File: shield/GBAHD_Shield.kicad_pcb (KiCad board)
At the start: 2 copper layers, 49 x 39 mm, 18 parts, among them J1 Conn_01x40, J2 Conn_02x08_Top_Bottom, J3 Conn_01x16, J4 Conn_02x10_Top_Bottom, J5 Conn_01x05, J6 Conn_02x03_Odd_Even, J7 Conn_01x01, SW1 SW_Push, U1 SNES_7PIN, U2 ATmega328P-AU, U3 WAS3157B, X1 Crystal_GND2

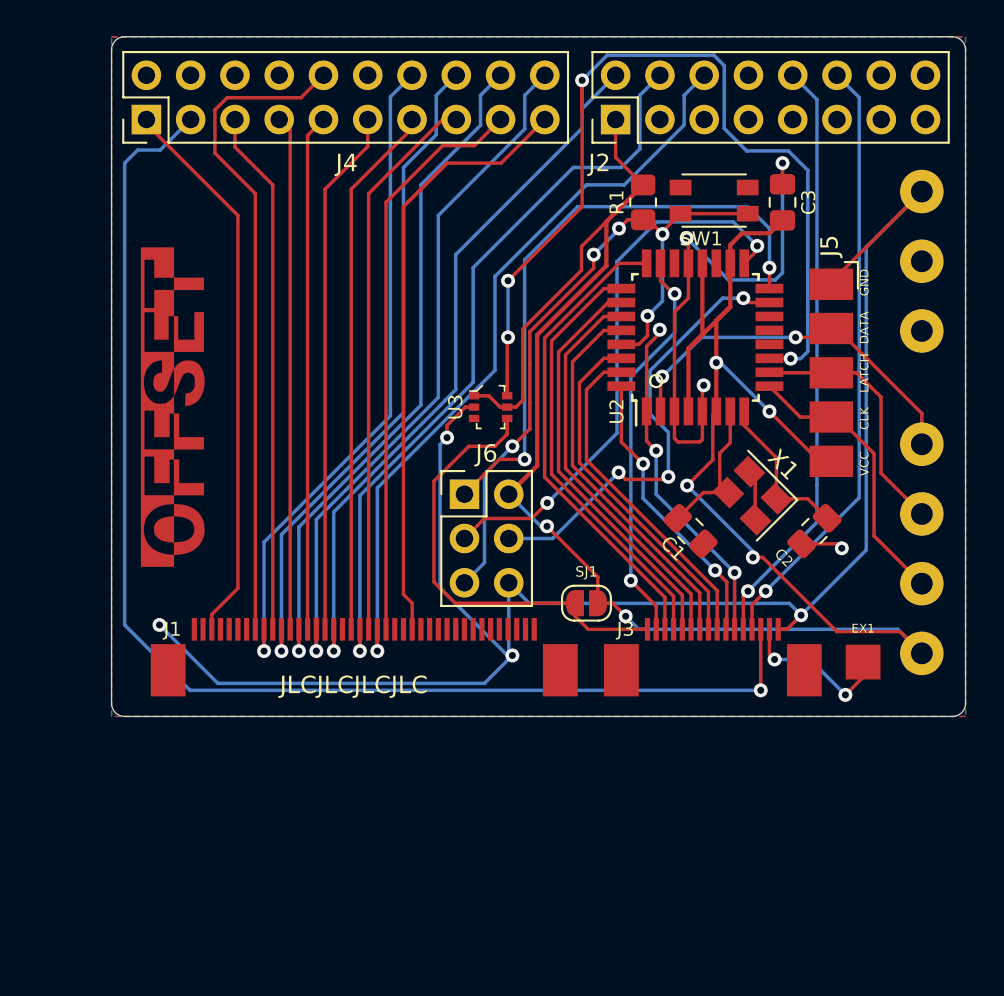
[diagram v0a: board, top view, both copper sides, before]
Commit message: Updated shield PCB and readme
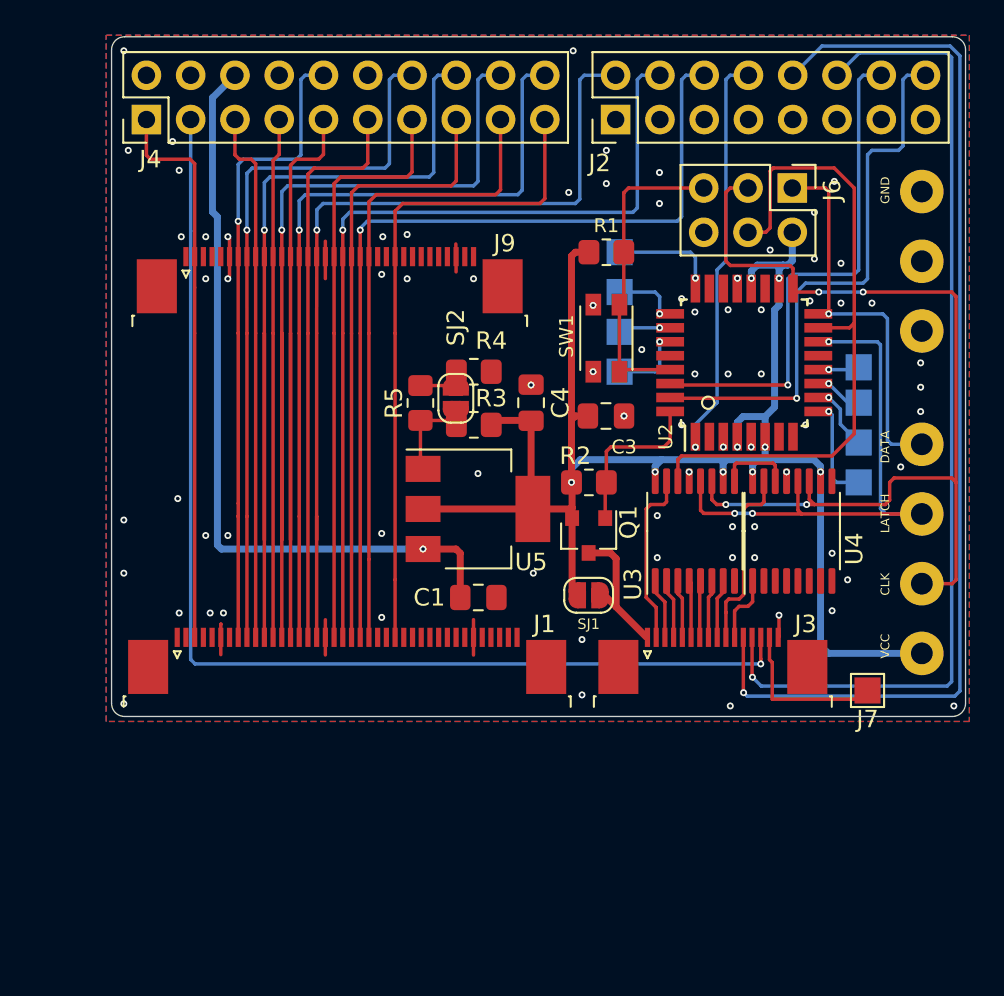
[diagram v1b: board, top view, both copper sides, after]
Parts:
- removed C2: 22pF, Capacitor_SMD:C_0805_2012Metric_Pad1.18x1.45mm_HandSolder
- removed G***: LOGO, OFFSET:OFFSET_LOGO_4.0mm
- removed X1: Crystal_GND2, Crystal:Crystal_SMD_3225-4Pin_3.2x2.5mm
- added C4: 22u, Capacitor_SMD:C_0805_2012Metric_Pad1.18x1.45mm_HandSolder, F.Cu at (68.1, 47.5)
- added J10: Conn_01x01, TestPoint:TestPoint_Pad_1.5x1.5mm, B.Cu at (73.2, 41.1)
- added J11: Conn_01x01, TestPoint:TestPoint_Pad_1.5x1.5mm, B.Cu at (73.2, 45.7)
- added J12: Conn_01x01, TestPoint:TestPoint_Pad_1.5x1.5mm, B.Cu at (86.9, 52.1)
- added J13: Conn_01x01, TestPoint:TestPoint_Pad_1.5x1.5mm, B.Cu at (86.9, 47.5)
- added J15: Conn_01x01, TestPoint:TestPoint_Pad_1.5x1.5mm, B.Cu at (73.2, 38.9)
- added J16: Conn_01x01, TestPoint:TestPoint_Pad_1.5x1.5mm, B.Cu at (73.2, 43.4)
- added J18: Conn_01x01, TestPoint:TestPoint_Pad_1.5x1.5mm, B.Cu at (86.9, 49.8)
- added J9: FLEX_GBA-SP, Connector_FFC-FPC:TE_3-1734839-4_1x34-1MP_P0.5mm_Horizontal, F.Cu at (56.5, 40.5)
- added Q1: Q_PMOS_GSD, Package_TO_SOT_SMD:SOT-23, F.Cu at (71.4, 55.1)
- added R2: 10K, Resistor_SMD:R_0805_2012Metric_Pad1.20x1.40mm_HandSolder, F.Cu at (71.4, 52.1)
- added R3: 10K, Resistor_SMD:R_0805_2012Metric_Pad1.20x1.40mm_HandSolder, F.Cu at (64.8, 48.8)
- added R4: 16.2K, Resistor_SMD:R_0805_2012Metric_Pad1.20x1.40mm_HandSolder, F.Cu at (64.8, 45.7)
- added R5: 7.5K, Resistor_SMD:R_0805_2012Metric_Pad1.20x1.40mm_HandSolder, F.Cu at (61.7, 47.5)
- added SJ2: SOLDER_JUMPER, Jumper:SolderJumper-2_P1.3mm_Open_RoundedPad1.0x1.5mm, F.Cu at (63.8, 47.2)
- added U4: 74HC595, Package_SO:TSSOP-16_4.4x5mm_P0.65mm, F.Cu at (83.1, 54.9)
- added U5: AMS1117, Package_TO_SOT_SMD:SOT-223-3_TabPin2, F.Cu at (65.0, 53.6)
- C1: value 22pF -> 100nF
- J1: value Conn_01x40 -> FFC_OGBA; footprint OFFSET:JUSHUO_AFC07-S40FCC-00 -> Connector_FFC-FPC:TE_4-1734839-0_1x40-1MP_P0.5mm_Horizontal
- J3: footprint OFFSET:JUSHUO_AFC07-S16FCC-00 -> Connector_FFC-FPC:TE_1-1734839-6_1x16-1MP_P0.5mm_Horizontal
- J5: value Conn_01x05 -> Conn_01x01; footprint OFFSET:Pads_01x05 -> TestPoint:TestPoint_Pad_1.5x1.5mm; moved to B.Cu
- J7: footprint OFFSET:SOLDER_PAD -> TestPoint:TestPoint_Pad_1.5x1.5mm
- U3: value WAS3157B -> 74HC595; footprint OFFSET:SOT-363 -> Package_SO:TSSOP-16_4.4x5mm_P0.65mm
- moved J6 25.7 mm to (83.1, 35.2), turned to 270 degrees
- moved C3 15.9 mm to (72.4, 48.3), turned to 180 degrees
- moved U3 13.7 mm to (77.5, 54.9), turned to 90 degrees
- moved C1 12.8 mm to (65.0, 58.7), turned to 180 degrees
- moved SW1 10.0 mm to (72.4, 43.8), turned to 270 degrees
- moved R1 3.56 mm to (72.4, 38.9), turned to 0 degrees
- moved U2 3.15 mm to (80.3, 45.2)
- moved J5 1.89 mm to (86.9, 45.5), turned to 0 degrees
- moved J7 1.80 mm to (87.4, 64.0), turned to 180 degrees
- moved J1 0.76 mm to (57.5, 62.3)
- moved SJ1 0.47 mm to (71.4, 58.5)
- moved J3 0.06 mm to (78.5, 62.3)
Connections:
- C1 pad 2: Net-(C1-Pad2) -> +5V
- C3 pad 2: SP_3V3 -> VCC
- J1 pad 1: Net-(J1-Pad1) -> (no net)
- J1 pad 18: Net-(J1-Pad18) -> GND
- J1 pad 2: Net-(J1-Pad2) -> (no net)
- J1 pad 24: Net-(J1-Pad24) -> (no net)
- J1 pad 25: Net-(J1-Pad25) -> (no net)
- J1 pad 27: Net-(J1-Pad27) -> (no net)
- J1 pad 28: Net-(J1-Pad28) -> (no net)
- J1 pad 29: Net-(J1-Pad29) -> (no net)
- J1 pad 30: Net-(J1-Pad30) -> (no net)
- J1 pad 31: Net-(J1-Pad31) -> (no net)
- J1 pad 32: Net-(J1-Pad32) -> (no net)
- J1 pad 33: Net-(J1-Pad33) -> (no net)
- J1 pad 34: Net-(J1-Pad34) -> (no net)
- J1 pad 35: Net-(J1-Pad35) -> GND
- J1 pad 36: Net-(J1-Pad36) -> (no net)
- J1 pad 37: Net-(J1-Pad37) -> (no net)
- J1 pad 38: Net-(J1-Pad38) -> (no net)
- J1 pad 39: Net-(J1-Pad39) -> (no net)
- J1 pad 4: Net-(J1-Pad4) -> (no net)
- J1 pad 40: Net-(J1-Pad40) -> (no net)
- J1 pad 5: Net-(J1-Pad5) -> (no net)
- J1 pad 6: Net-(J1-Pad6) -> GND
- J1 pad 7: Net-(J1-Pad7) -> (no net)
- J2 pad 1: SP_3V3 -> (no net)
- J2 pad 11: Net-(J2-Pad11) -> (no net)
- J2 pad 13: Net-(J2-Pad13) -> (no net)
- J2 pad 15: Net-(J2-Pad15) -> (no net)
- J2 pad 16: SP_ARD0 -> RX
- J2 pad 5: Net-(J2-Pad5) -> (no net)
- J2 pad 7: Net-(J2-Pad7) -> (no net)
- J2 pad 8: SP_ARD4 -> PIXEL_GRID
- J2 pad 9: Net-(J2-Pad9) -> (no net)
- J4 pad 12: SP_ARD12 -> (no net)
- J4 pad 2: SP_ARD17 -> (no net)
- J4 pad 4: SP_ARD16 -> (no net)
- J4 pad 6: SP_ARD15 -> +5V
- J4 pad 8: SP_ARD14 -> (no net)
- J5 pad 1: GND -> Net-(J5-Pad1)
- J6 pad 2: SP_3V3 -> VCC
- R1 pad 1: SP_3V3 -> VCC
- SJ1 pad 1: GBA_VCC -> VCC
- SJ1 pad 2: SP_3V3 -> GBA_VCC
- U1 pad 1: SP_3V3 -> VCC
- U1 pad 2: SNS_CLK -> ICSP_SCK
- U1 pad 4: SNS_DATA -> ICSP_MISO
- U2 pad 1: GBA_SELECT -> PIXEL_GRID
- U2 pad 10: SNS_LATCH -> Net-(J18-Pad1)
- U2 pad 11: GBA_POWER_SEL -> Net-(J13-Pad1)
- U2 pad 12: Net-(U2-Pad12) -> Net-(J5-Pad1)
- U2 pad 13: Net-(U2-Pad13) -> (no net)
- U2 pad 14: Net-(U2-Pad14) -> SNS_LATCH
- U2 pad 18: SP_3V3 -> VCC
- U2 pad 19: Net-(U2-Pad19) -> (no net)
- U2 pad 2: SNS_DATA -> (no net)
- U2 pad 20: SP_3V3 -> VCC
- U2 pad 22: Net-(U2-Pad22) -> (no net)
- U2 pad 23: GBA_UP -> (no net)
- U2 pad 24: GBA_DOWN -> Net-(J15-Pad1)
- U2 pad 25: GBA_LEFT -> Net-(J10-Pad1)
- U2 pad 26: GBA_RGHT -> Net-(J16-Pad1)
- U2 pad 27: GBA_A -> Net-(J11-Pad1)
- U2 pad 28: GBA_B -> (no net)
- U2 pad 30: GBA_L -> SP_ARD1
- U2 pad 31: GBA_R -> RX
- U2 pad 32: GBA_START -> GBA_POWER_SEL
- U2 pad 4: SP_3V3 -> VCC
- U2 pad 6: SP_3V3 -> VCC
- U2 pad 7: Net-(C1-Pad2) -> (no net)
- U2 pad 8: Net-(C2-Pad2) -> (no net)
- U2 pad 9: SNS_CLK -> Net-(J12-Pad1)
- U3 pad 1: SP_3V3 -> GBA_DOWN
- U3 pad 2: GND -> GBA_LEFT
- U3 pad 3: Net-(U3-Pad3) -> GBA_RGHT
- U3 pad 4: GBA_VCC -> GBA_A
- U3 pad 5: SP_3V3 -> GBA_B
- U3 pad 6: GBA_POWER_SEL -> GBA_L
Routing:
- net SP_3V3: track 126.4 -> 0.00 mm, vias 6 -> 0
- net GND: track 134.3 -> 13.1 mm, vias 8 -> 78
- net VCC: track 0.00 -> 91.3 mm, vias 0 -> 9
- net +5V: track 0.00 -> 44.3 mm, vias 0 -> 1
- net GBA_POWER_SEL: track 52.9 -> 9.45 mm, vias 4 -> 0
- net RX: track 0.00 -> 32.3 mm, vias 0 -> 1
- net SP_ARD1: track 0.00 -> 29.5 mm, vias 0 -> 1
- net GBA_AUD2: track 34.1 -> 62.8 mm
- net ICSP_SCK: track 32.0 -> 56.3 mm, vias 2 -> 4
- net GBA_DOWN: track 27.2 -> 3.46 mm
- net PIXEL_GRID: track 0.00 -> 23.2 mm, vias 0 -> 1
- net AT_RST: track 40.4 -> 18.0 mm, vias 5 -> 0
- net GBA_AUD1: track 34.9 -> 57.1 mm
- net SNS_DATA: track 21.9 -> 0.00 mm, vias 2 -> 0
- net GBA_LEFT: track 24.7 -> 3.40 mm
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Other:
- net class Default: via_dia 0.8 -> 0.4; via_drill 0.4 -> 0.2
- net class VCC: trace_width 0.25 -> 0.4; via_dia 0.8 -> 0.4; via_drill 0.4 -> 0.2
- rule via_min_drill: 0.3 -> 0.2
- board text added: "Designed in Germany"
- board text added: "ManCloud 2021"
- board text added: "v20210318"
- board text removed: "Designed in México"
- board text removed: "EX1"
- board text removed: "JLCJLCJLCJLC"
- board text removed: "Raizu 2020"

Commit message: Updated to "Full-Shield"
* changed supplies to 3V3 and 4V0
* added pads for BAT connection
* added 32-Pin FFC Connector
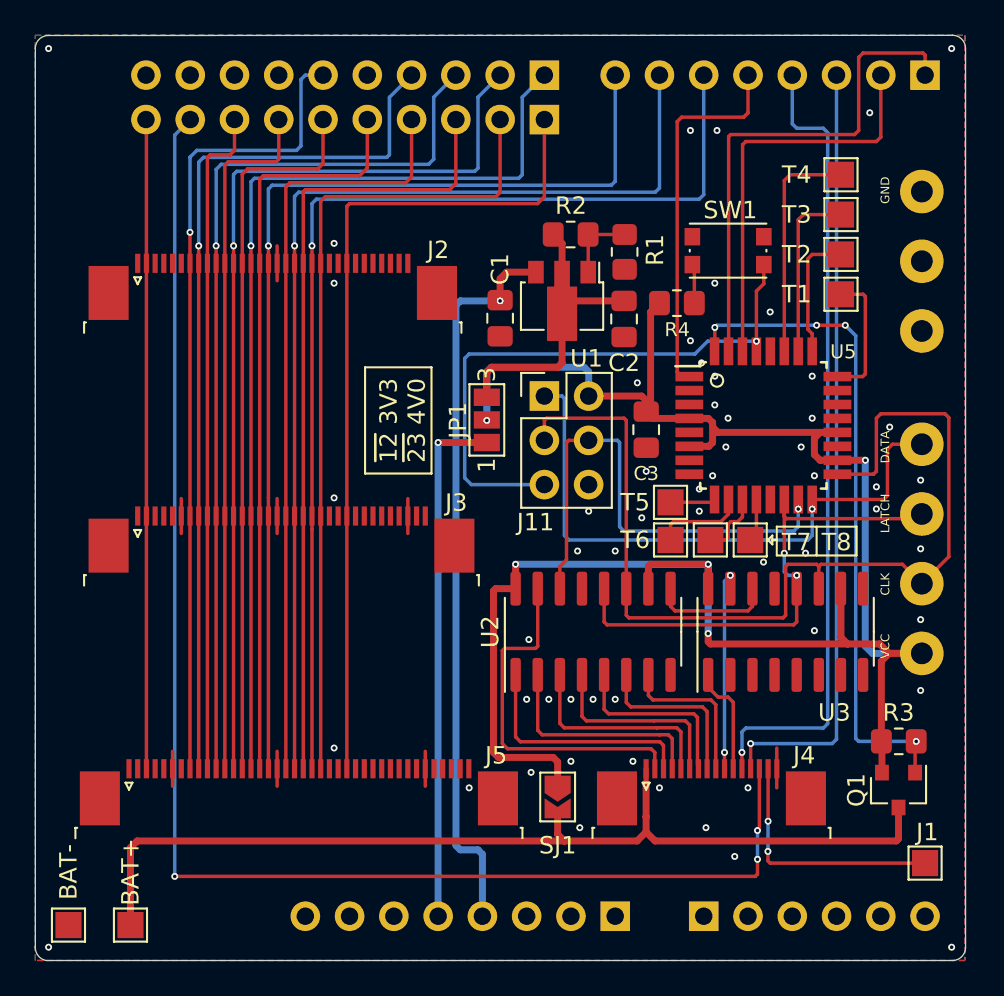
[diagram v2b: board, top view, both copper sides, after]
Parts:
- removed C4: 22u, Capacitor_SMD:C_0805_2012Metric_Pad1.18x1.45mm_HandSolder
- removed J12, J13, J16, J18: Conn_01x01, TestPoint:TestPoint_Pad_1.5x1.5mm
- removed the R3 at (64.8, 48.8)
- removed the R4 at (64.8, 45.7)
- removed R5: 7.5K, Resistor_SMD:R_0805_2012Metric_Pad1.20x1.40mm_HandSolder
- removed SJ2: SOLDER_JUMPER, Jumper:SolderJumper-2_P1.3mm_Open_RoundedPad1.0x1.5mm
- removed the U4 at (83.1, 54.9)
- added BAT+: Conn_01x01, TestPoint:TestPoint_Pad_1.5x1.5mm, F.Cu at (45.1, 77.5)
- added BAT-: Conn_01x01, TestPoint:TestPoint_Pad_1.5x1.5mm, F.Cu at (41.5, 77.5)
- added C2: 22u, Capacitor_SMD:C_0805_2012Metric_Pad1.18x1.45mm_HandSolder, F.Cu at (73.4, 42.7)
- added J6: Conn_01x06, Connector_PinHeader_2.54mm:PinHeader_1x06_P2.54mm_Vertical, B.Cu at (78.0, 77.0)
- added J7: Conn_01x08, Connector_PinHeader_2.54mm:PinHeader_1x08_P2.54mm_Vertical, B.Cu at (72.9, 77.0)
- added J8: Conn_01x10, Connector_PinHeader_2.54mm:PinHeader_1x10_P2.54mm_Vertical, B.Cu at (68.8, 31.2)
- added JP1: SolderJumper_3_Open, Jumper:SolderJumper-3_P1.3mm_Open_Pad1.0x1.5mm_NumberLabels, F.Cu at (65.5, 48.5)
- added R1: 2.2k, Resistor_SMD:R_0805_2012Metric_Pad1.20x1.40mm_HandSolder, F.Cu at (73.4, 38.8)
- added R2: 1k, Resistor_SMD:R_0805_2012Metric_Pad1.20x1.40mm_HandSolder, F.Cu at (70.3, 37.8)
- added T2: Conn_01x01, TestPoint:TestPoint_Pad_1.5x1.5mm, F.Cu at (85.9, 39.0)
- added T3: Conn_01x01, TestPoint:TestPoint_Pad_1.5x1.5mm, F.Cu at (85.9, 36.7)
- added T5: Conn_01x01, TestPoint:TestPoint_Pad_1.5x1.5mm, F.Cu at (76.1, 53.2)
- added T6: Conn_01x01, TestPoint:TestPoint_Pad_1.5x1.5mm, F.Cu at (76.1, 55.4)
- added T7: Conn_01x01, TestPoint:TestPoint_Pad_1.5x1.5mm, F.Cu at (78.4, 55.4)
- added U1: AZ1117R-ADJ, Package_TO_SOT_SMD:SOT-89-3, F.Cu at (69.8, 41.7)
- J10: value Conn_01x01 -> Conn_01x10; footprint TestPoint:TestPoint_Pad_1.5x1.5mm -> Connector_PinHeader_2.54mm:PinHeader_1x10_P2.54mm_Vertical
- J2: value Conn_02x08_Top_Bottom -> FFC_OGBA_32; footprint Connector_PinHeader_2.54mm:PinHeader_2x08_P2.54mm_Vertical -> Connector_FFC-FPC:TE_3-1734839-2_1x32-1MP_P0.5mm_Horizontal
- J3: value Conn_01x16 -> FFC_GBA-SP; footprint Connector_FFC-FPC:TE_1-1734839-6_1x16-1MP_P0.5mm_Horizontal -> Connector_FFC-FPC:TE_3-1734839-4_1x34-1MP_P0.5mm_Horizontal
- J4: value Conn_02x10_Top_Bottom -> Conn_01x16; footprint Connector_PinHeader_2.54mm:PinHeader_2x10_P2.54mm_Vertical -> Connector_FFC-FPC:TE_1-1734839-6_1x16-1MP_P0.5mm_Horizontal
- J5: renamed from J1; value FFC_OGBA -> FFC_OGBA_40
- J9: value FLEX_GBA-SP -> Conn_01x08; footprint Connector_FFC-FPC:TE_3-1734839-4_1x34-1MP_P0.5mm_Horizontal -> Connector_PinHeader_2.54mm:PinHeader_1x08_P2.54mm_Vertical; moved to B.Cu
- SJ1: footprint Jumper:SolderJumper-2_P1.3mm_Open_RoundedPad1.0x1.5mm -> Jumper:SolderJumper-2_P1.3mm_Open_TrianglePad1.0x1.5mm
- SW1: footprint OFFSET:XKB-TS-1185EC-C-D-B -> Button_Switch_SMD:SW_Push_1P1T_NO_CK_KMR2
- T1: renamed from J15; moved to F.Cu
- T4: renamed from J11; moved to F.Cu
- T8: renamed from J5; moved to F.Cu
- U2: value ATmega328P-AU -> 74HC595; footprint Package_QFP:TQFP-32_7x7mm_P0.8mm -> Package_SO:SOIC-16_3.9x9.9mm_P1.27mm
- U3: footprint Package_SO:TSSOP-16_4.4x5mm_P0.65mm -> Package_SO:SOIC-16_3.9x9.9mm_P1.27mm
- U5: value AMS1117 -> ATmega328P-AU; footprint Package_TO_SOT_SMD:SOT-223-3_TabPin2 -> Package_QFP:TQFP-32_7x7mm_P0.8mm
- moved J4 50.4 mm to (78.4, 69.8), turned to 0 degrees
- moved J9 36.1 mm to (90.7, 28.7), turned to 90 degrees
- moved J3 25.7 mm to (53.8, 55.4)
- moved R3 23.2 mm to (89.2, 66.9)
- moved Q1 23.0 mm to (89.2, 69.7)
- moved J2 21.9 mm to (53.2, 40.9), turned to 0 degrees
- moved J11 18.6 mm to (68.8, 47.1), turned to 0 degrees
- moved U2 17.7 mm to (71.6, 60.6)
- moved U5 17.1 mm to (81.4, 48.8)
- moved T4 17.0 mm to (85.9, 34.4)
- moved C1 16.1 mm to (66.3, 42.7), turned to 90 degrees
- moved J10 13.2 mm to (68.8, 28.7), turned to 90 degrees
- moved T1 12.9 mm to (85.9, 41.3)
- moved SJ1 11.7 mm to (69.6, 70.1), turned to 270 degrees
- moved T8 11.7 mm to (80.6, 55.4)
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- renumbered J7 to J1, J6 to J11, R2 to R3, R1 to R4, U1 to U4
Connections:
- J1 pad 1: Net-(J3-Pad15) -> Net-(J1-Pad1)
- J10 pad 1: Net-(J10-Pad1) -> GB_G3
- J2 pad 10: GBA_AUD2 -> GB_R2
- J2 pad 11: (no net) -> GB_R1
- J2 pad 12: GBA_AUD1 -> GB_G5
- J2 pad 13: (no net) -> GB_G4
- J2 pad 14: SP_ARD1 -> GB_G3
- J2 pad 15: (no net) -> GB_G2
- J2 pad 16: RX -> GB_G1
- J2 pad 2: GB_G1 -> GB_DCLK
- J2 pad 3: GND -> (no net)
- J2 pad 4: GB_B4 -> (no net)
- J2 pad 6: GB_B2 -> (no net)
- J2 pad 7: (no net) -> GB_R5
- J2 pad 8: PIXEL_GRID -> GB_R4
- J2 pad 9: (no net) -> GB_R3
- J3 pad 1: GBA_VCC -> (no net)
- J3 pad 10: GBA_START -> GB_R2
- J3 pad 11: GBA_SELECT -> GB_R1
- J3 pad 12: GBA_AUD2 -> GB_G5
- J3 pad 13: GBA_AUD1 -> GB_G4
- J3 pad 14: GBA_CLK -> GB_G3
- J3 pad 15: Net-(J3-Pad15) -> GB_G2
- J3 pad 16: GND -> GB_G1
- J3 pad 2: GBA_UP -> GB_DCLK
- J3 pad 3: GBA_DOWN -> (no net)
- J3 pad 4: GBA_LEFT -> (no net)
- J3 pad 5: GBA_RGHT -> (no net)
- J3 pad 6: GBA_A -> GND
- J3 pad 7: GBA_B -> GB_R5
- J3 pad 8: GBA_L -> GB_R4
- J3 pad 9: GBA_R -> GB_R3
- J4 pad 1: GB_DCLK -> GBA_VCC
- J4 pad 10: GB_R5 -> GBA_START
- J4 pad 11: GB_G2 -> GBA_SELECT
- J4 pad 12: (no net) -> GBA_AUD2
- J4 pad 13: GB_B5 -> GBA_AUD1
- J4 pad 14: GB_R4 -> GBA_CLK
- J4 pad 15: GB_B3 -> Net-(J1-Pad1)
- J4 pad 16: GB_R2 -> GND
- J4 pad 2: (no net) -> GBA_UP
- J4 pad 3: GBA_CLK -> GBA_DOWN
- J4 pad 4: (no net) -> GBA_LEFT
- J4 pad 5: GB_R3 -> GBA_RGHT
- J4 pad 6: +5V -> GBA_A
- J4 pad 7: GB_R1 -> GBA_B
- J4 pad 8: (no net) -> GBA_L
- J4 pad 9: GB_G4 -> GBA_R
- J9 pad 1: (no net) -> RX
- J9 pad 2: GB_DCLK -> SP_ARD1
- J9 pad 3: (no net) -> GBA_AUD1
- J9 pad 4: (no net) -> GBA_AUD2
- J9 pad 5: (no net) -> PIXEL_GRID
- J9 pad 6: GND -> GB_B2
- J9 pad 7: GB_R5 -> GB_B4
- J9 pad 8: GB_R4 -> GB_G1
- T1 pad 1: Net-(J15-Pad1) -> Net-(T1-Pad1)
- T4 pad 1: Net-(J11-Pad1) -> Net-(T4-Pad1)
- T8 pad 1: Net-(J5-Pad1) -> Net-(T8-Pad1)
- U2 pad 1: PIXEL_GRID -> GBA_DOWN
- U2 pad 10: Net-(J18-Pad1) -> VCC
- U2 pad 11: Net-(J13-Pad1) -> ICSP_SCK
- U2 pad 12: Net-(J5-Pad1) -> SNS_LATCH
- U2 pad 13: (no net) -> GND
- U2 pad 14: SNS_LATCH -> ICSP_MOSI
- U2 pad 15: ICSP_MOSI -> GBA_UP
- U2 pad 16: ICSP_MISO -> VCC
- U2 pad 2: (no net) -> GBA_LEFT
- U2 pad 3: GND -> GBA_RGHT
- U2 pad 4: VCC -> GBA_A
- U2 pad 5: GND -> GBA_B
- U2 pad 6: VCC -> GBA_L
- U2 pad 7: (no net) -> GBA_R
- U2 pad 8: (no net) -> GND
- U2 pad 9: Net-(J12-Pad1) -> QH_OUT-SER_IN
- U3 pad 1: GBA_DOWN -> GBA_SELECT
- U3 pad 14: ICSP_MOSI -> QH_OUT-SER_IN
- U3 pad 15: GBA_UP -> GBA_START
- U3 pad 2: GBA_LEFT -> (no net)
- U3 pad 3: GBA_RGHT -> (no net)
- U3 pad 4: GBA_A -> (no net)
- U3 pad 5: GBA_B -> (no net)
- U3 pad 6: GBA_L -> (no net)
- U3 pad 7: GBA_R -> (no net)
- U3 pad 9: QH_OUT-SER_IN -> (no net)
- U5 pad 1: Net-(R3-Pad2) -> PIXEL_GRID
- U5 pad 2: VCC -> (no net)
- U5 pad 3: +5V -> GND
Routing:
- net GBA_VCC: track 8.16 -> 56.0 mm
- net +3V3: track 0.00 -> 30.0 mm, vias 0 -> 1
- net GBA_POWER_SEL: track 9.45 -> 38.2 mm, vias 0 -> 4
- net VCC: track 91.3 -> 115.3 mm, vias 9 -> 5
- net AT_RST: track 18.0 -> 36.1 mm, vias 0 -> 1
- net GBA_CLK: track 65.3 -> 83.4 mm, vias 1 -> 3
- net +4V: track 0.00 -> 17.1 mm
- net GBA_AUD2: track 62.8 -> 46.2 mm
- net Net-(J1-Pad1): track 0.00 -> 14.4 mm, vias 0 -> 2
- net Net-(T4-Pad1): track 0.00 -> 13.2 mm
- net GBA_AUD1: track 57.1 -> 44.6 mm
- net ICSP_MISO: track 21.7 -> 34.2 mm
- net GBA_UP: track 10.1 -> 20.7 mm
- net GB_B4: track 49.9 -> 60.5 mm
- net GB_B2: track 51.5 -> 62.0 mm
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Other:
- board size 49 x 39 mm -> 53.4 x 53.1 mm
- board text added: "ManCloud 2021 Designed in Germany v20210321"
- board text added: "~12~ 3V3 ~23~ 4V0"
- board text removed: "Designed in Germany"
- board text removed: "ManCloud 2021"
- board text removed: "v20210318"

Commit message: Major Updates
* Added QSB for GBA SP
* Fixed wrong supply voltare for Components in case of SP setup
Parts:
- renumbered BAT+ to BAT+1, BAT- to BAT-1
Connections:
- C3 pad 2: VCC -> +3V3
- J11 pad 2: VCC -> +3V3
- R4 pad 1: VCC -> +3V3
- U2 pad 10: VCC -> +3V3
- U2 pad 13: GND -> ~GBA_BUTTONS_EN~
- U2 pad 16: VCC -> +3V3
- U3 pad 10: VCC -> +3V3
- U3 pad 13: GND -> ~GBA_BUTTONS_EN~
- U3 pad 16: VCC -> +3V3
- U4 pad 1: VCC -> +3V3
- U5 pad 13: (no net) -> ~GBA_BUTTONS_EN~
- U5 pad 18: VCC -> +3V3
- U5 pad 20: VCC -> +3V3
- U5 pad 4: VCC -> +3V3
- U5 pad 6: VCC -> +3V3
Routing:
- net +3V3: track 30.0 -> 123.9 mm, vias 1 -> 6
- net VCC: track 115.3 -> 47.7 mm, vias 5 -> 2
- net ~GBA_BUTTONS_EN~: track 0.00 -> 21.3 mm, vias 0 -> 2
- net GBA_VCC: track 56.0 -> 56.5 mm
- net GND: vias 56 -> 60
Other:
- board text added: "ManCloud 2021 Designed in Germany v20210406"
- board text removed: "ManCloud 2021 Designed in Germany v20210321"
